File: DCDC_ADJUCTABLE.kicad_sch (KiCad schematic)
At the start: 42 parts, among them Q3001 IRLML5103, Q3002 NVTFWS4D9N04XMTAG, Q3003 NVTFWS4D9N04XMTAG, U3001 TPS62933, U3002 TPS62933, U3003 LM74700, U3004 LM74700

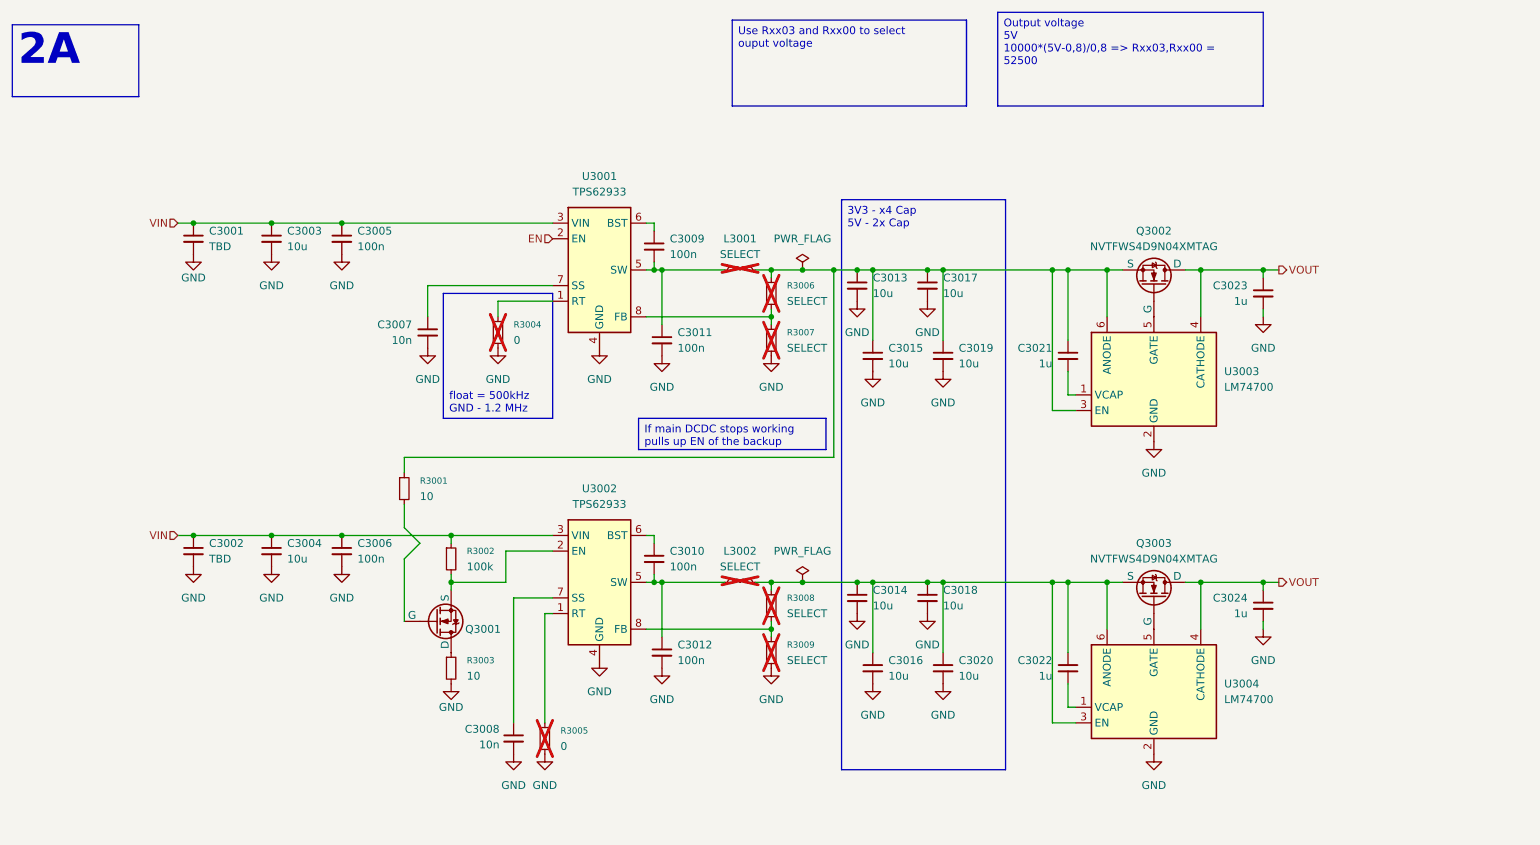
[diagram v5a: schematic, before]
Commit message: added universal switch, added simples current source, reworked test schematic and pcb
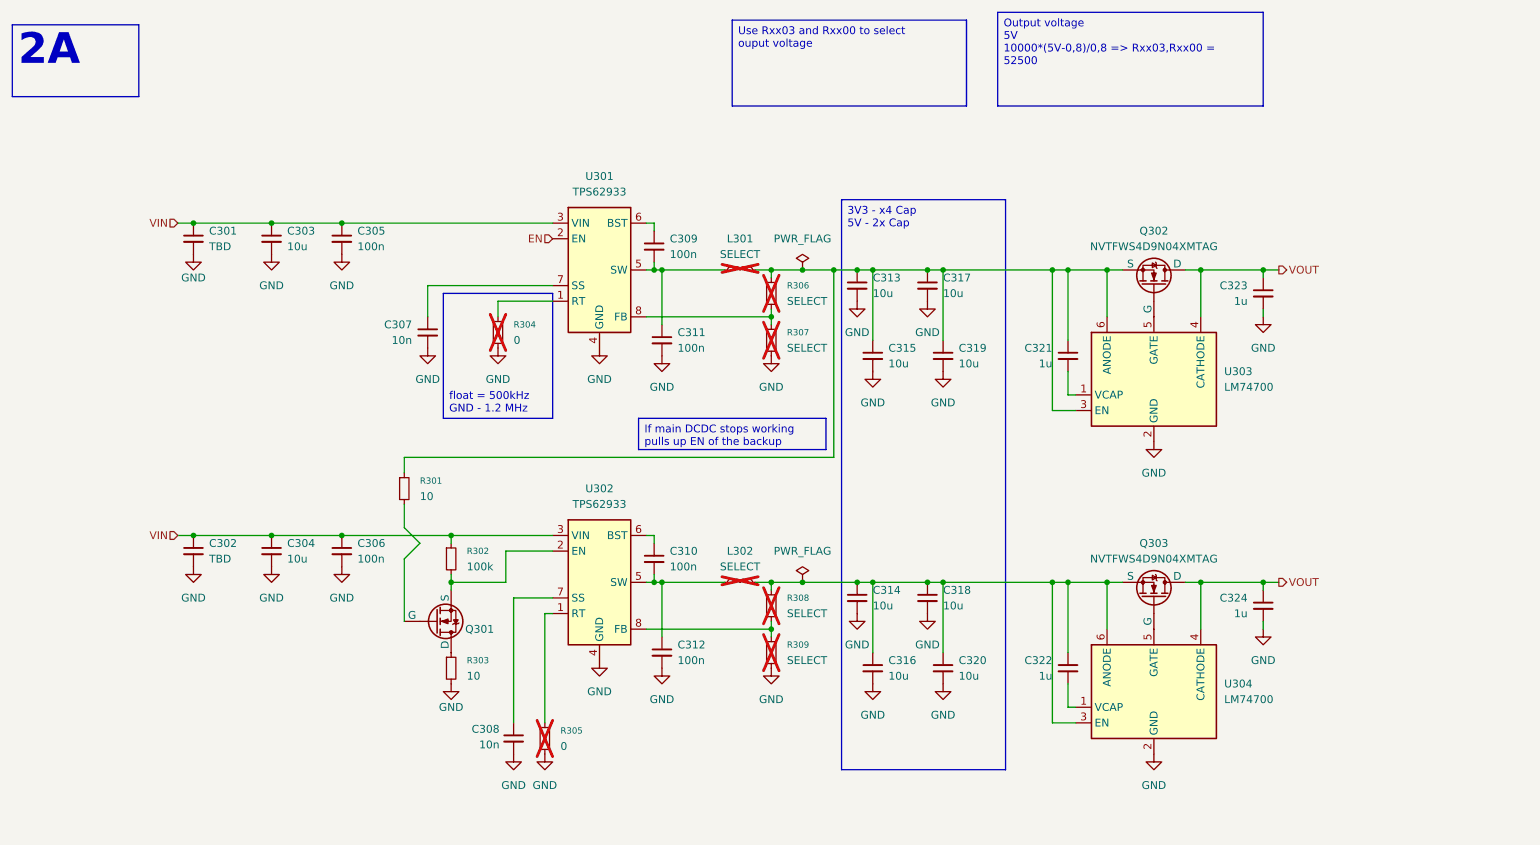
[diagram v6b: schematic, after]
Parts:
- L301: renamed from L3001; footprint Inductor_SMD:L_Vishay_IHLP-2525 -> Inductor_SMD:L_6.3x6.3_H3
- L302: renamed from L3002; footprint Inductor_SMD:L_Vishay_IHLP-2525 -> Inductor_SMD:L_6.3x6.3_H3
- renumbered C3001 to C301, C3002 to C302, C3003 to C303, C3004 to C304, C3005 to C305, C3006 to C306, C3007 to C307, C3008 to C308, C3009 to C309, C3010 to C310, C3011 to C311, C3012 to C312, C3013 to C313, C3014 to C314, C3015 to C315, C3016 to C316, C3017 to C317, C3018 to C318, C3019 to C319, C3020 to C320, C3021 to C321, C3022 to C322, C3023 to C323, C3024 to C324, Q3001 to Q301, Q3002 to Q302, Q3003 to Q303, R3001 to R301, R3002 to R302, R3003 to R303, R3004 to R304, R3005 to R305, R3006 to R306, R3007 to R307, R3008 to R308, R3009 to R309, U3001 to U301, U3002 to U302, U3003 to U303, U3004 to U304

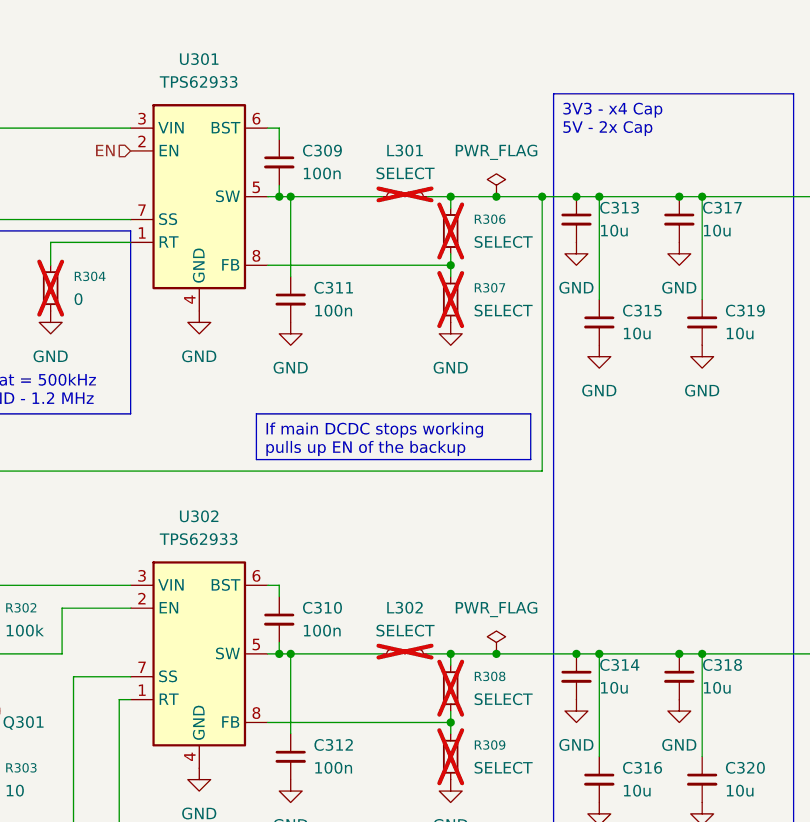
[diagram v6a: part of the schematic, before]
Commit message: specified inductors
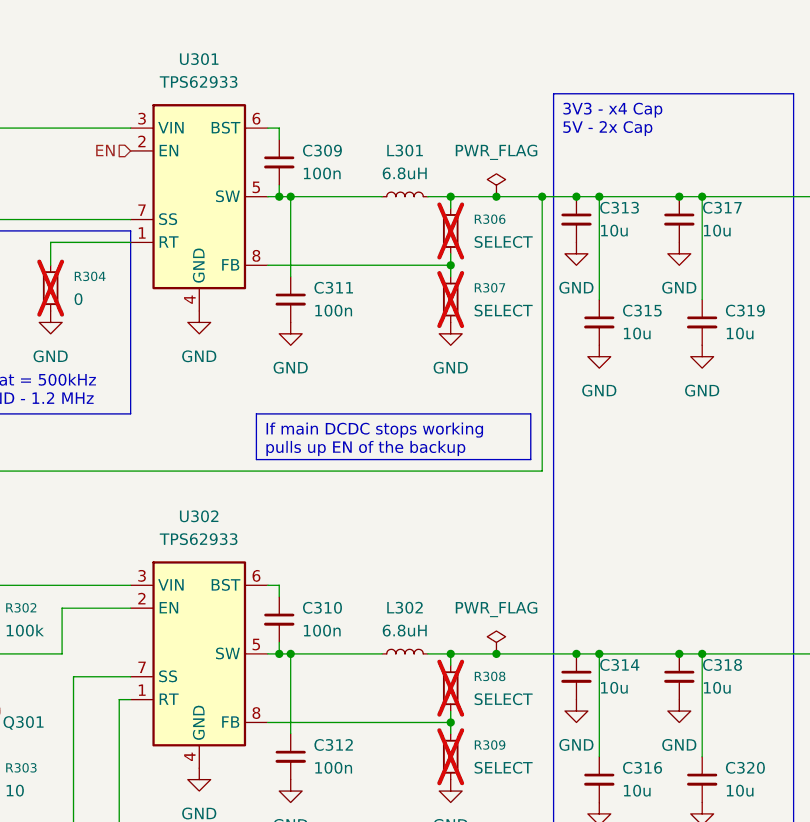
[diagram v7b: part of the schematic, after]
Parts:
- L301, L302: value SELECT -> 6.8uH; footprint Inductor_SMD:L_6.3x6.3_H3 -> Inductor_SMD:L_Bourns_SRR1260; now fitted
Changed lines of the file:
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@@
 	)
 	(symbol
-		(lib_id "Device:L_Small")
-		(at 135.89 120.65 90)
-		(unit 1)
-		(exclude_from_sim no)
-		(in_bom yes)
-		(on_board yes)
-		(dnp yes)
-		(fields_autoplaced yes)
-		(property "Reference" "L302"
-			(at 135.89 115.57 90)
-			(effects
-				(font
-					(size 1.27 1.27)
-				)
-			)
-		)
-		(property "Value" "SELECT"
-			(at 135.89 118.11 90)
-			(effects
-				(font
-					(size 1.27 1.27)
-				)
-			)
-		)
-		(property "Footprint" "Inductor_SMD:L_6.3x6.3_H3"
-			(at 135.89 120.65 0)
-			(effects
-				(font
-					(size 1.27 1.27)
-				)
-				(hide yes)
-			)
-		)
-		(property "Datasheet" "~"
-			(at 135.89 120.65 0)
-			(effects
-				(font
-					(size 1.27 1.27)
-				)
-				(hide yes)
-			)
-		)
-		(property "Description" "Inductor, small symbol"
-			(at 135.89 120.65 0)
-			(effects
-				(font
-					(size 1.27 1.27)
-				)
-				(hide yes)
-			)
-		)
-		(pin "1"
-		)
-		(pin "2"
-		)
-		(instances
-			(project "TEST_PCB"
-				(path "/29496ace-b476-4f24-a65f-9da1dd70122c/ab9854e7-c9d1-48ce-8906-c016083b51c2"
-					(reference "L1202")
-					(unit 1)
-				)
-				(path "/29496ace-b476-4f24-a65f-9da1dd70122c/59fca87d-eab6-4325-93c7-8130e49f891e/591fb6d7-fa0b-4828-8f5f-2b4a43bbf0dc"
-					(reference "L302")
-					(unit 1)
-				)
-			)
-			(project "EPS_CORE"
-				(path "/43e5e7c8-e7e0-4528-9a3e-b1557849918d/ce55ed75-3d20-4bd3-84d2-d62dbd0d02de/591fb6d7-fa0b-4828-8f5f-2b4a43bbf0dc"
-					(reference "L?")
-					(unit 1)
-				)
-			)
-			(project "EPS"
-				(path "/94201994-47b8-4213-8d1a-05da12b2a7b0/2939b268-15b7-411b-af55-ccc6daa126bc/0a6a38f5-f1fa-4783-be04-d08625b52ef4"
-					(reference "L3002")
-					(unit 1)
-				)
-				(path "/94201994-47b8-4213-8d1a-05da12b2a7b0/2939b268-15b7-411b-af55-ccc6daa126bc/60831aa8-2fd3-4f26-86cf-bb066e732cb3"
-					(reference "L3102")
-					(unit 1)
-				)
-				(path "/94201994-47b8-4213-8d1a-05da12b2a7b0/2939b268-15b7-411b-af55-ccc6daa126bc/6931fe57-8e65-4211-9bc6-ecb270a394b8"
-					(reference "L3202")
-					(unit 1)
-				)
-				(path "/94201994-47b8-4213-8d1a-05da12b2a7b0/2939b268-15b7-411b-af55-ccc6daa126bc/a2a2e8b0-eb98-4edc-81c6-6014879aa93c"
-					(reference "L4202")
-					(unit 1)
-				)
-				(path "/94201994-47b8-4213-8d1a-05da12b2a7b0/447ec425-294e-4947-a7f3-941020b4706e/ce55ed75-3d20-4bd3-84d2-d62dbd0d02de/591fb6d7-fa0b-4828-8f5f-2b4a43bbf0dc"
-					(reference "L8702")
-					(unit 1)
-				)
-			)
-			(project "EPS_OUTPUT_CHANNELS"
-				(path "/c9173887-04ec-4c2a-a5a4-b6a694df57d5/0a6a38f5-f1fa-4783-be04-d08625b52ef4"
-					(reference "L8002")
-					(unit 1)
-				)
-				(path "/c9173887-04ec-4c2a-a5a4-b6a694df57d5/60831aa8-2fd3-4f26-86cf-bb066e732cb3"
-					(reference "L8102")
-					(unit 1)
-				)
-				(path "/c9173887-04ec-4c2a-a5a4-b6a694df57d5/6931fe57-8e65-4211-9bc6-ecb270a394b8"
-					(reference "L8202")
-					(unit 1)
-				)
-				(path "/c9173887-04ec-4c2a-a5a4-b6a694df57d5/a2a2e8b0-eb98-4edc-81c6-6014879aa93c"
-					(reference "L9202")
-					(unit 1)
-				)
-			)
-		)
-	)
-	(symbol
 		(lib_id "power:GND")
 		(at 168.91 86.36 0)
@@
 	)
 	(symbol
+		(lib_id "Device:L_Small")
+		(at 135.89 120.65 90)
+		(unit 1)
+		(exclude_from_sim no)
+		(in_bom yes)
+		(on_board yes)
+		(dnp no)
+		(fields_autoplaced yes)
+		(property "Reference" "L302"
+			(at 135.89 115.57 90)
+			(effects
+				(font
+					(size 1.27 1.27)
+				)
+			)
+		)
+		(property "Value" "6.8uH"
+			(at 135.89 118.11 90)
+			(effects
+				(font
+					(size 1.27 1.27)
+				)
+			)
+		)
+		(property "Footprint" "Inductor_SMD:L_Bourns_SRR1260"
+			(at 135.89 120.65 0)
+			(effects
+				(font
+					(size 1.27 1.27)
+				)
+				(hide yes)
+			)
+		)
+		(property "Datasheet" "https://cz.mouser.com/datasheet/3/40/1/SRR1260A.pdf"
+			(at 135.89 120.65 0)
+			(effects
+				(font
+					(size 1.27 1.27)
+				)
+				(hide yes)
+			)
+		)
+		(property "Description" "SRR1260A-6R8Y"
+			(at 135.89 120.65 0)
+			(effects
+				(font
+					(size 1.27 1.27)
+				)
+				(hide yes)
+			)
+		)
+		(pin "1"
+		)
+		(pin "2"
+		)
+		(instances
+			(project "TEST_PCB"
+				(path "/29496ace-b476-4f24-a65f-9da1dd70122c/ab9854e7-c9d1-48ce-8906-c016083b51c2"
+					(reference "L1101")
+					(unit 1)
+				)
+				(path "/29496ace-b476-4f24-a65f-9da1dd70122c/59fca87d-eab6-4325-93c7-8130e49f891e/591fb6d7-fa0b-4828-8f5f-2b4a43bbf0dc"
+					(reference "L302")
+					(unit 1)
+				)
+			)
+		)
+	)
+	(symbol
 		(lib_id "Regulator_Switching:TPS62933")
 		(at 113.03 69.85 0)
@@
 		(in_bom yes)
 		(on_board yes)
-		(dnp yes)
+		(dnp no)
 		(fields_autoplaced yes)
 		(property "Reference" "L301"
@@
 			)
 		)
-		(property "Value" "SELECT"
+		(property "Value" "6.8uH"
 			(at 135.89 67.31 90)
 			(effects
@@
 			)
 		)
-		(property "Footprint" "Inductor_SMD:L_6.3x6.3_H3"
+		(property "Footprint" "Inductor_SMD:L_Bourns_SRR1260"
 			(at 135.89 69.85 0)
 			(effects
@@
 			)
 		)
-		(property "Datasheet" "~"
+		(property "Datasheet" "https://cz.mouser.com/datasheet/3/40/1/SRR1260A.pdf"
 			(at 135.89 69.85 0)
 			(effects
@@
 			)
 		)
-		(property "Description" "Inductor, small symbol"
+		(property "Description" "SRR1260A-6R8Y"
 			(at 135.89 69.85 0)
 			(effects

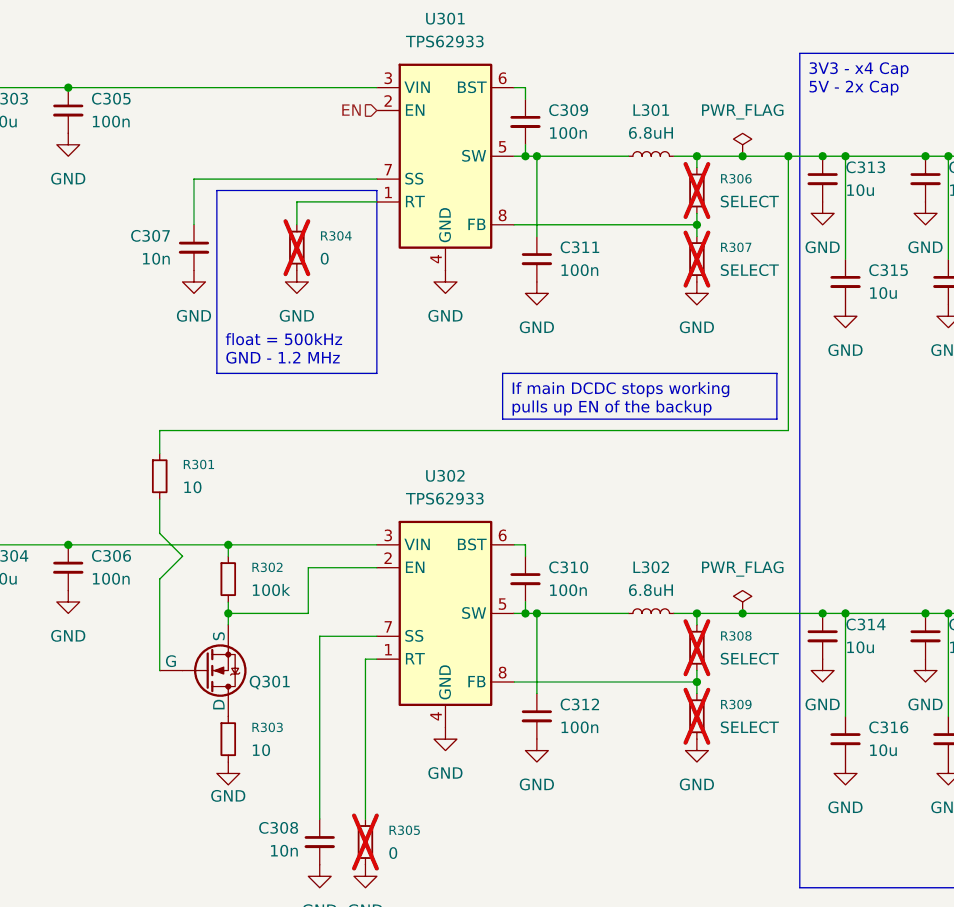
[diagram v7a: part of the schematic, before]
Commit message: Minor changes to acomodate jlcpcb guidelines, this version ordered
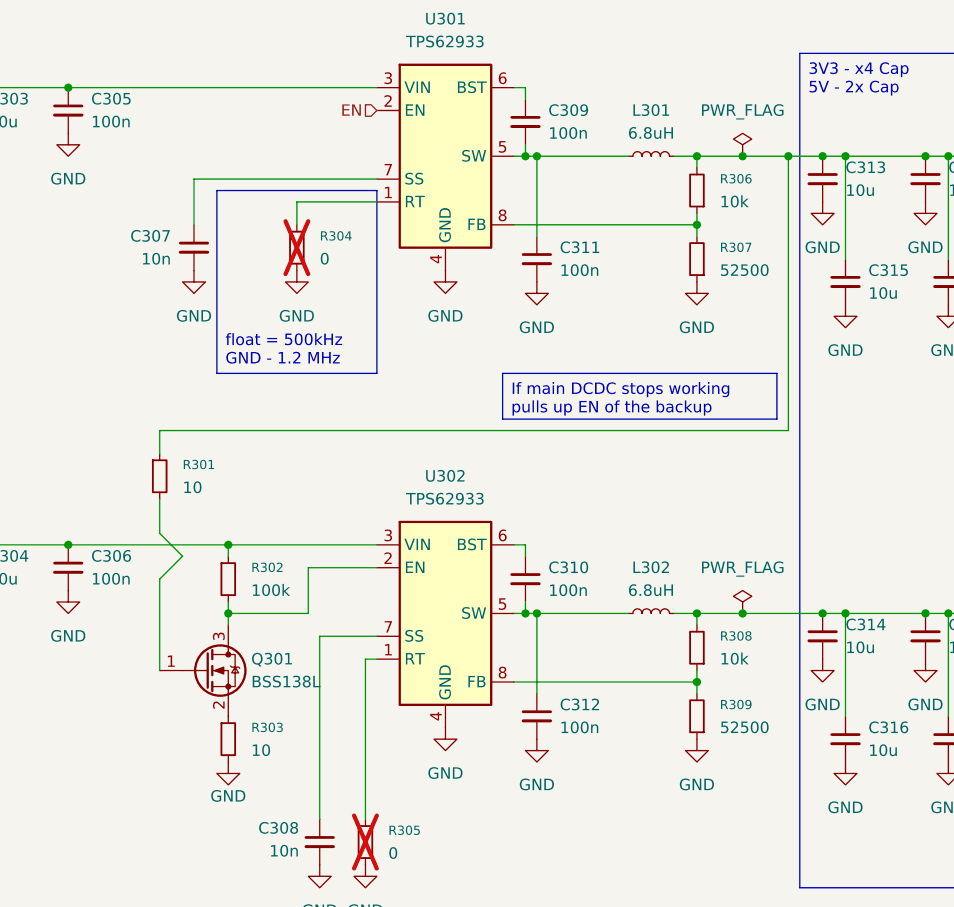
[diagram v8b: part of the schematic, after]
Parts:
- removed Q301: IRLML5103, Package_TO_SOT_SMD:SOT-23, symbol Simulation_SPICE:NMOS
- added Q301: BSS138L, Package_TO_SOT_SMD:SOT-23, symbol VZLU_Transistor_FET:IRLML2803TRPBF
- C303, C304, C313, C314, C315, C316, C317, C318, C319, C320: footprint Capacitor_SMD:C_0603_1608Metric_Pad1.08x0.95mm_HandSolder -> Capacitor_SMD:C_1206_3216Metric_Pad1.33x1.80mm_HandSolder
- R306, R308: value SELECT -> 10k; now fitted
- R307, R309: value SELECT -> 52500; now fitted
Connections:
- net at R303.1: now also Q301.2 (S)
- net at R301.2: now also Q301.1 (G)
- net at R302.2, U302.2 (EN): now also Q301.3 (D)
